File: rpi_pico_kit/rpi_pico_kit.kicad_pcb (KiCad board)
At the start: 2 copper layers, 244 parts, among them J1 DC Jack 5.5x2.1mm, J10 OLED Display SSD1306, J11 Conn_01x04_Male, J12 Conn_01x04_Male, J13 AudioJack-CUI-SJ-3523-SMT, J14 AudioJack-CUI-SJ-3523-SMT, J2 USB_B, J3 Conn_01x03_Male, J4 DB15_Female_HighDensity_Mount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, J5 HDMI_A, J6 Conn_01x08_Male, J7 Conn_01x08_Male, J8 Conn_01x08_Male, J9 Micro_SD_Card_Det, Q1 DMN63D8L-7, Q2 DMN63D8L-7, Q3 DMN63D8L-7, Q4 DMN63D8L-7, Q5 DMN63D8L-7, Q6 DMN63D8L-7, Q7 DMN63D8L-7, SW1 SW_Push, SW10 SW_Push, SW2 RotaryEncoder_Switch, SW3 SW_Push, SW4 SW_Push, SW5 SW_Push, SW6 SW_Push, SW7 SW_Push, SW8 SW_Push, SW9 SW_Push, U1 RPi Pico, U10 74LVC2G34GV, U11 PCM5101A, U2 NCP1117-3.3_SOT223, U3 RP2040, U4 W25Q16JVSSIQ, U5 74HC14, U6 74HC14, U7 MCP23S08-xSO, U8 AT24CS32, U9 NCP115-3.3_SOT23-5, Y1 12MHz

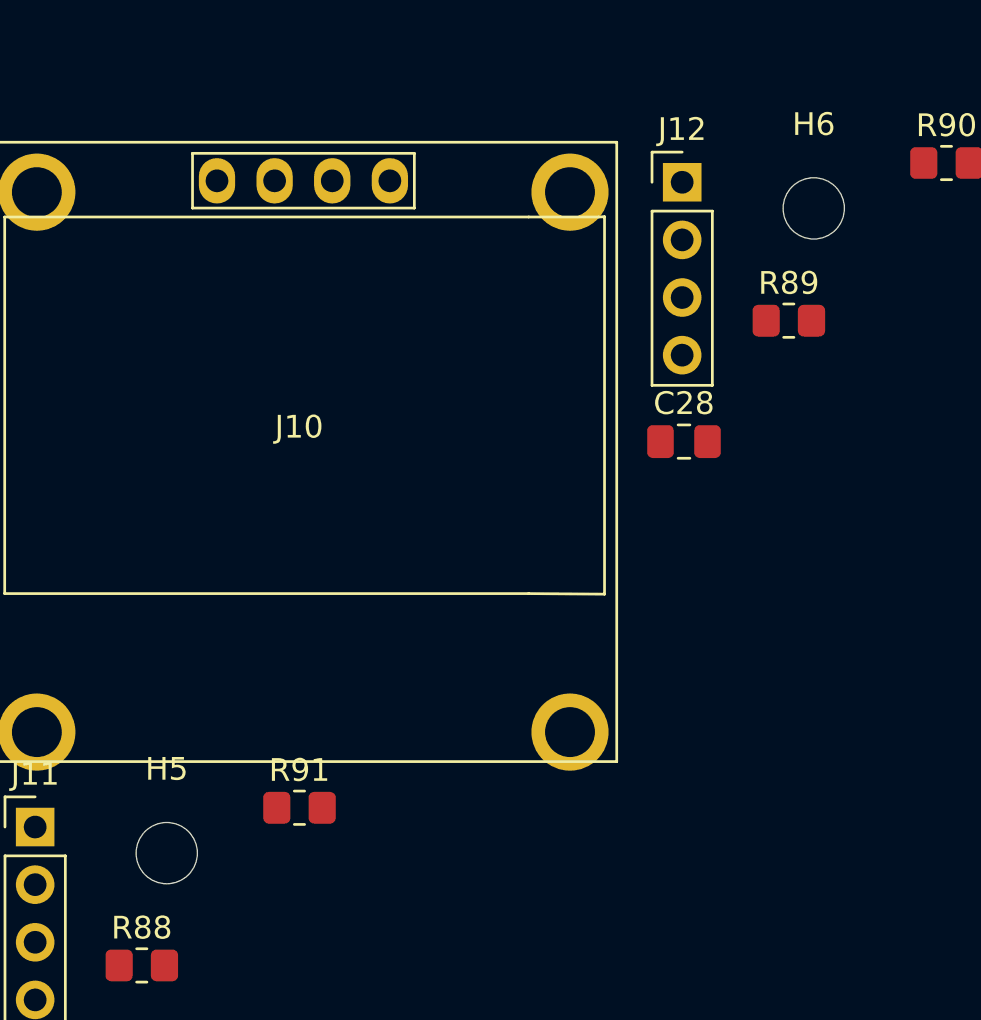
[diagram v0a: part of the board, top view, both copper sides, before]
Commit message: removed additional holes for oled
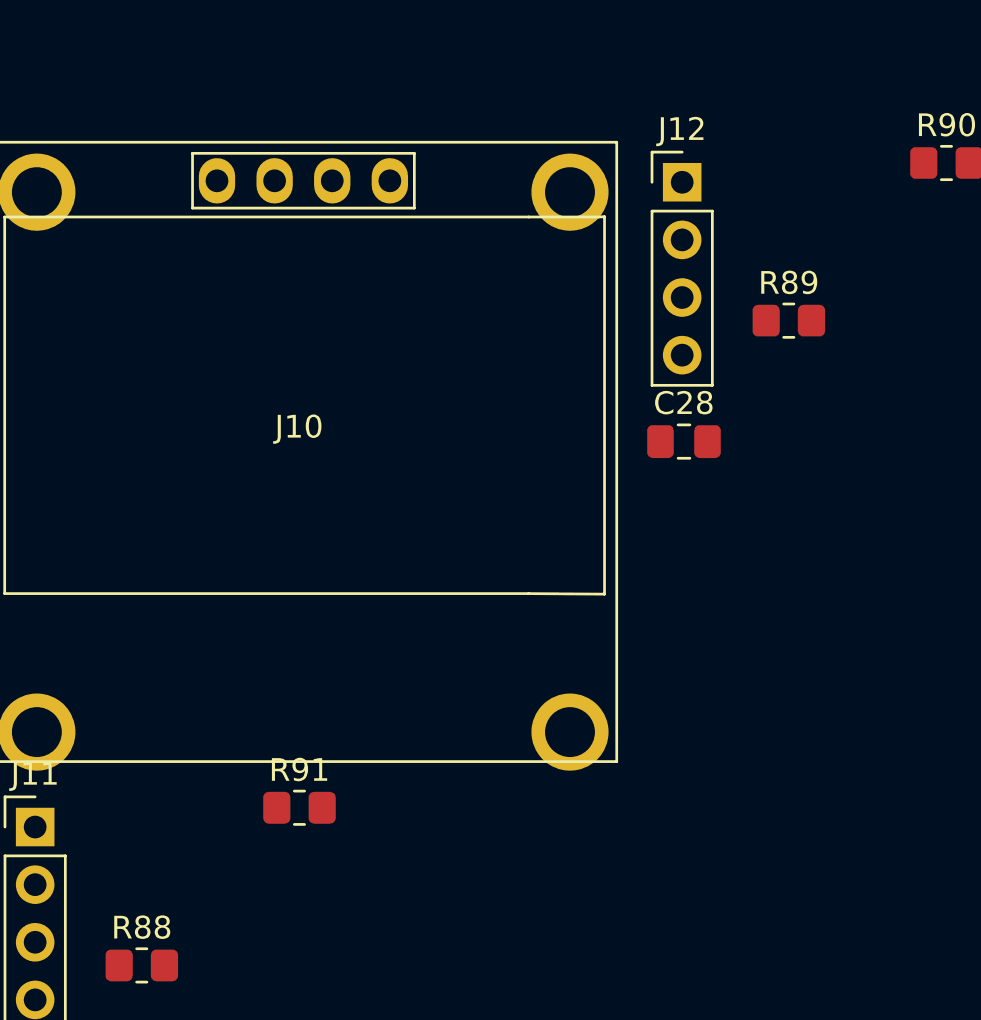
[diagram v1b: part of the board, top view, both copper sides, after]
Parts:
- removed H5, H6: MountingHole, MountingHole:MountingHole_2.7mm_M2.5
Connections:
- J10 pad 1: GND -> unconnected-(J10-GND)
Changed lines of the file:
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@@
   (net 210 "unconnected-(U7-INT)")
   (net 211 "unconnected-(U9-NC)")
+  (net 212 "unconnected-(J10-GND)")
   (footprint "Resistor_SMD:R_0805_2012Metric_Pad1.20x1.40mm_HandSolder" (layer "F.Cu")
     (at 158.5692 106.0422)
@@
     )
   )
-  (footprint "MountingHole:MountingHole_2.7mm_M2.5" (layer "F.Cu")
-    (at 177.1692 51.5222)
-    (descr "Mounting Hole 2.7mm, no annular, M2.5")
-    (tags "mounting hole 2.7mm no annular m2.5")
-    (property "Manufacturer Part Number" "~")
-    (property "Sheetfile" "i2c_devices.kicad_sch")
-    (property "Sheetname" "I2C Devices")
-    (property "Supplier" "~")
-    (property "Supplier Part URL" "~")
-    (attr exclude_from_pos_files)
-    (fp_text reference "H5" (at 0 -3.7) (layer "F.SilkS")
-        (effects (font (size 1 1) (thickness 0.15)))
-    )
-    (fp_text value "MountingHole" (at 0 3.7) (layer "F.Fab")
-        (effects (font (size 1 1) (thickness 0.15)))
-    )
-    (fp_text user "${REFERENCE}" (at 0 0) (layer "F.Fab")
-        (effects (font (size 1 1) (thickness 0.15)))
-    )
-    (fp_circle (center 0 0) (end 2.7 0)
-      (stroke (width 0.15) (type solid)) (fill none) (layer "Cmts.User"))
-    (fp_circle (center 0 0) (end 2.95 0)
-      (stroke (width 0.05) (type solid)) (fill none) (layer "F.CrtYd"))
-    (pad "" np_thru_hole circle (at 0 0) (size 2.7 2.7) (drill 2.7) (layers *.Cu *.Mask))
-  )
   (footprint "Custom:SW_SPST_Omron_B3FS-100xP_12" (layer "F.Cu")
     (at 34.6092 74.8622)
@@
     )
   )
-  (footprint "MountingHole:MountingHole_2.7mm_M2.5" (layer "F.Cu")
-    (at 205.6892 23.1022)
-    (descr "Mounting Hole 2.7mm, no annular, M2.5")
-    (tags "mounting hole 2.7mm no annular m2.5")
-    (property "Manufacturer Part Number" "~")
-    (property "Sheetfile" "i2c_devices.kicad_sch")
-    (property "Sheetname" "I2C Devices")
-    (property "Supplier" "~")
-    (property "Supplier Part URL" "~")
-    (attr exclude_from_pos_files)
-    (fp_text reference "H6" (at 0 -3.7) (layer "F.SilkS")
-        (effects (font (size 1 1) (thickness 0.15)))
-    )
-    (fp_text value "MountingHole" (at 0 3.7) (layer "F.Fab")
-        (effects (font (size 1 1) (thickness 0.15)))
-    )
-    (fp_text user "${REFERENCE}" (at 0 0) (layer "F.Fab")
-        (effects (font (size 1 1) (thickness 0.15)))
-    )
-    (fp_circle (center 0 0) (end 2.7 0)
-      (stroke (width 0.15) (type solid)) (fill none) (layer "Cmts.User"))
-    (fp_circle (center 0 0) (end 2.95 0)
-      (stroke (width 0.05) (type solid)) (fill none) (layer "F.CrtYd"))
-    (pad "" np_thru_hole circle (at 0 0) (size 2.7 2.7) (drill 2.7) (layers *.Cu *.Mask))
-  )
   (footprint "Connector_BarrelJack:BarrelJack_GCT_DCJ200-10-A_Horizontal" (layer "F.Cu")
     (at 62.5892 21.6522)
@@
       (stroke (width 0.05) (type default)) (fill none) (layer "F.CrtYd"))
     (pad "1" thru_hole oval (at -3.62 -10.6 90) (size 2 1.6) (drill 1) (layers *.Cu *.Mask)
-      (net 3 "GND") (pinfunction "GND") (pintype "input"))
+      (net 212 "unconnected-(J10-GND)") (pinfunction "GND") (pintype "input"))
     (pad "2" thru_hole oval (at -1.08 -10.6 90) (size 2 1.6) (drill 1) (layers *.Cu *.Mask)
       (net 1 "+3V3") (pinfunction "VCC") (pintype "input"))

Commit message: initial changes in pcb, drawn pcb outline
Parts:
- moved C1 390.2 mm to (-142.3, -0.30)
- moved C10 390.2 mm to (-150.6, 8.23)
- moved C11 390.2 mm to (-137.5, -0.30)
- moved C12 390.2 mm to (-142.3, 2.71)
- moved C13 390.2 mm to (-160.1, 16.0)
- moved C14 390.2 mm to (-140.8, -3.31)
- moved C15 390.2 mm to (-132.4, -8.86)
- moved C16 390.2 mm to (-160.1, 19.1)
- moved C17 390.2 mm to (-160.1, 22.1)
- moved C18 390.2 mm to (-155.3, 16.0)
- moved C2 390.2 mm to (-127.6, -8.86)
- moved C3 390.2 mm to (-157.3, 11.1)
- moved C4 390.2 mm to (-145.8, 8.23)
- moved C5 390.2 mm to (-169.4, 33.5)
- moved C6 390.2 mm to (-136.0, -3.31)
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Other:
- board outline added: 149.9 x 99.1 mm

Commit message: filtered controls and indicators
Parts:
- moved J14 294.0 mm to (129.5, 74.2)
- moved SW9 287.7 mm to (102.2, 130.2)
- moved J10 279.7 mm to (167.0, 68.6)
- moved J13 278.3 mm to (115.2, 74.8)
- moved SW10 269.8 mm to (116.2, 130.2)
- moved LED5 262.5 mm to (161.9, 113.0)
- moved J11 259.5 mm to (144.8, 114.9)
- moved SW5 257.7 mm to (156.8, 131.4)
- moved SW6 253.4 mm to (168.9, 131.4)
- moved J9 253.1 mm to (84.5, 105.1)
- moved SW4 246.0 mm to (144.8, 131.4)
- moved SW7 245.5 mm to (75.6, 130.2)
- moved BZ1 244.2 mm to (90.2, 76.2)
- moved LED7 242.5 mm to (161.9, 120.7)
- moved J2 241.0 mm to (66.1, 49.7), turned to 90 degrees
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
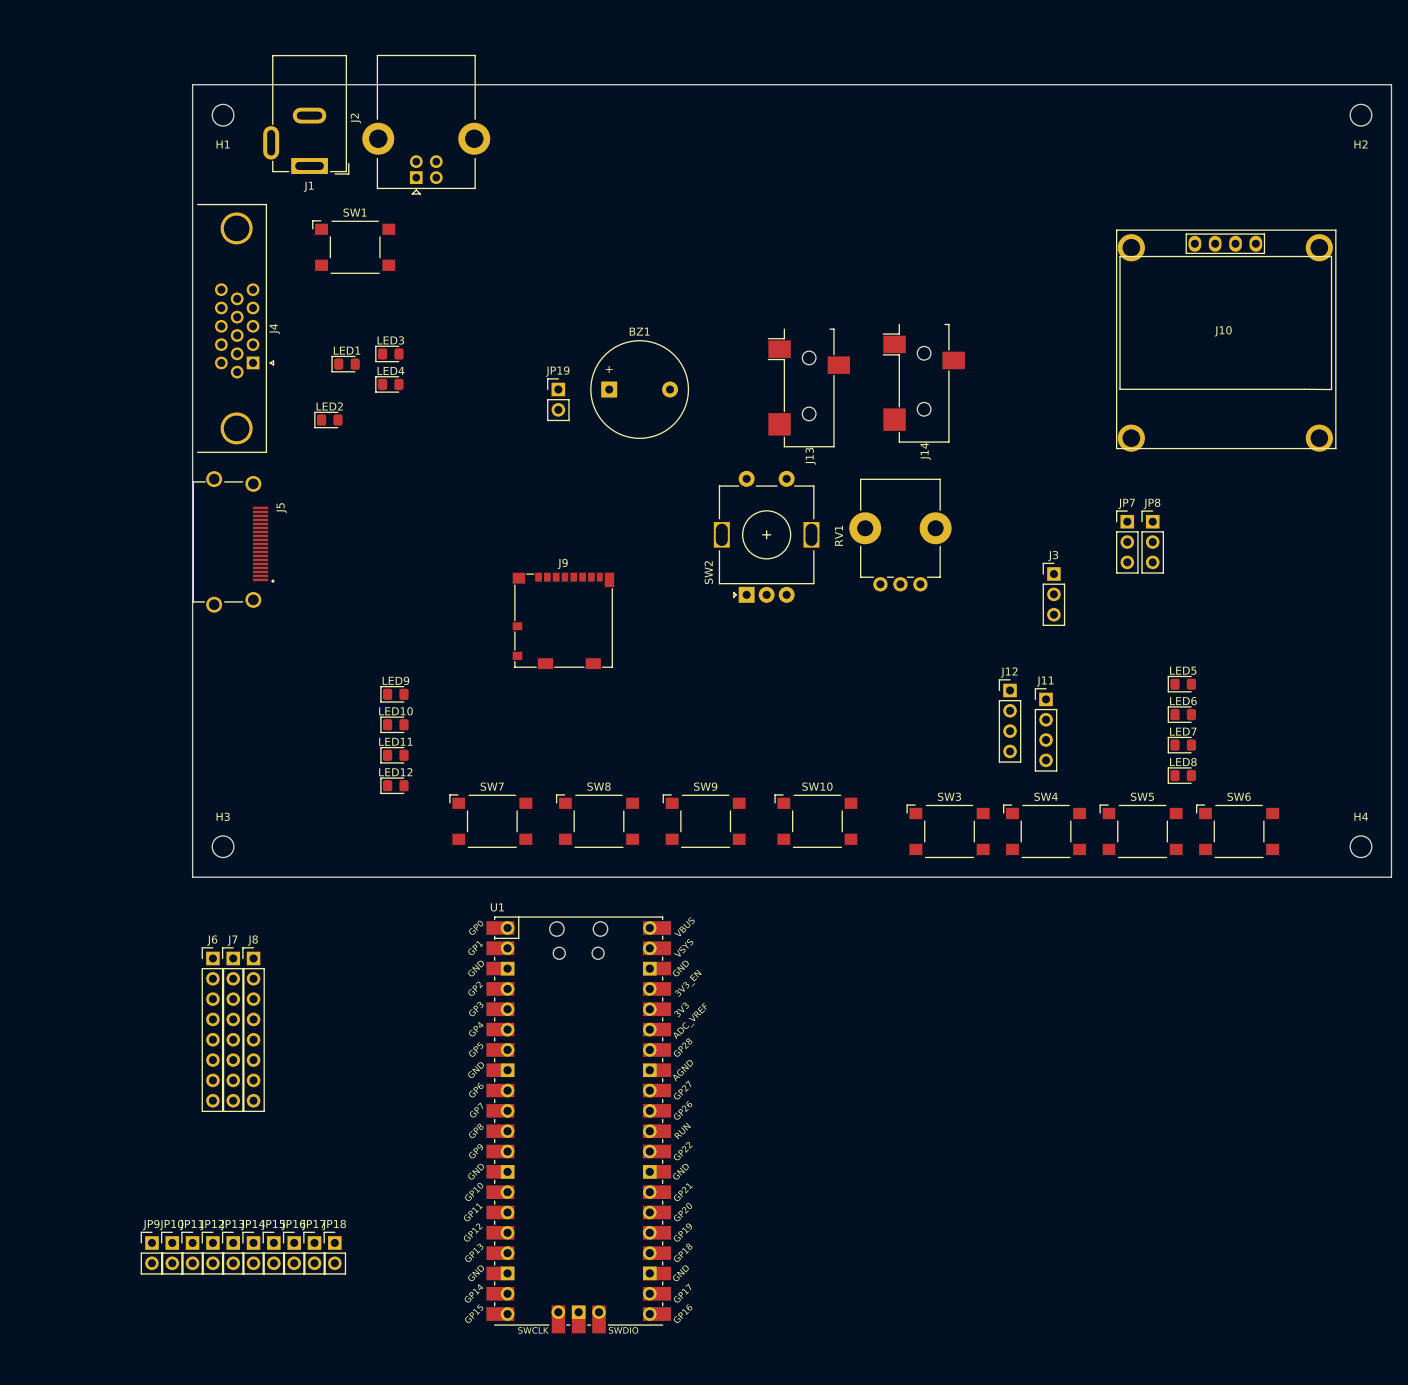
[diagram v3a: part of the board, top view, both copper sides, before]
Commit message: changed position of controls and indicators
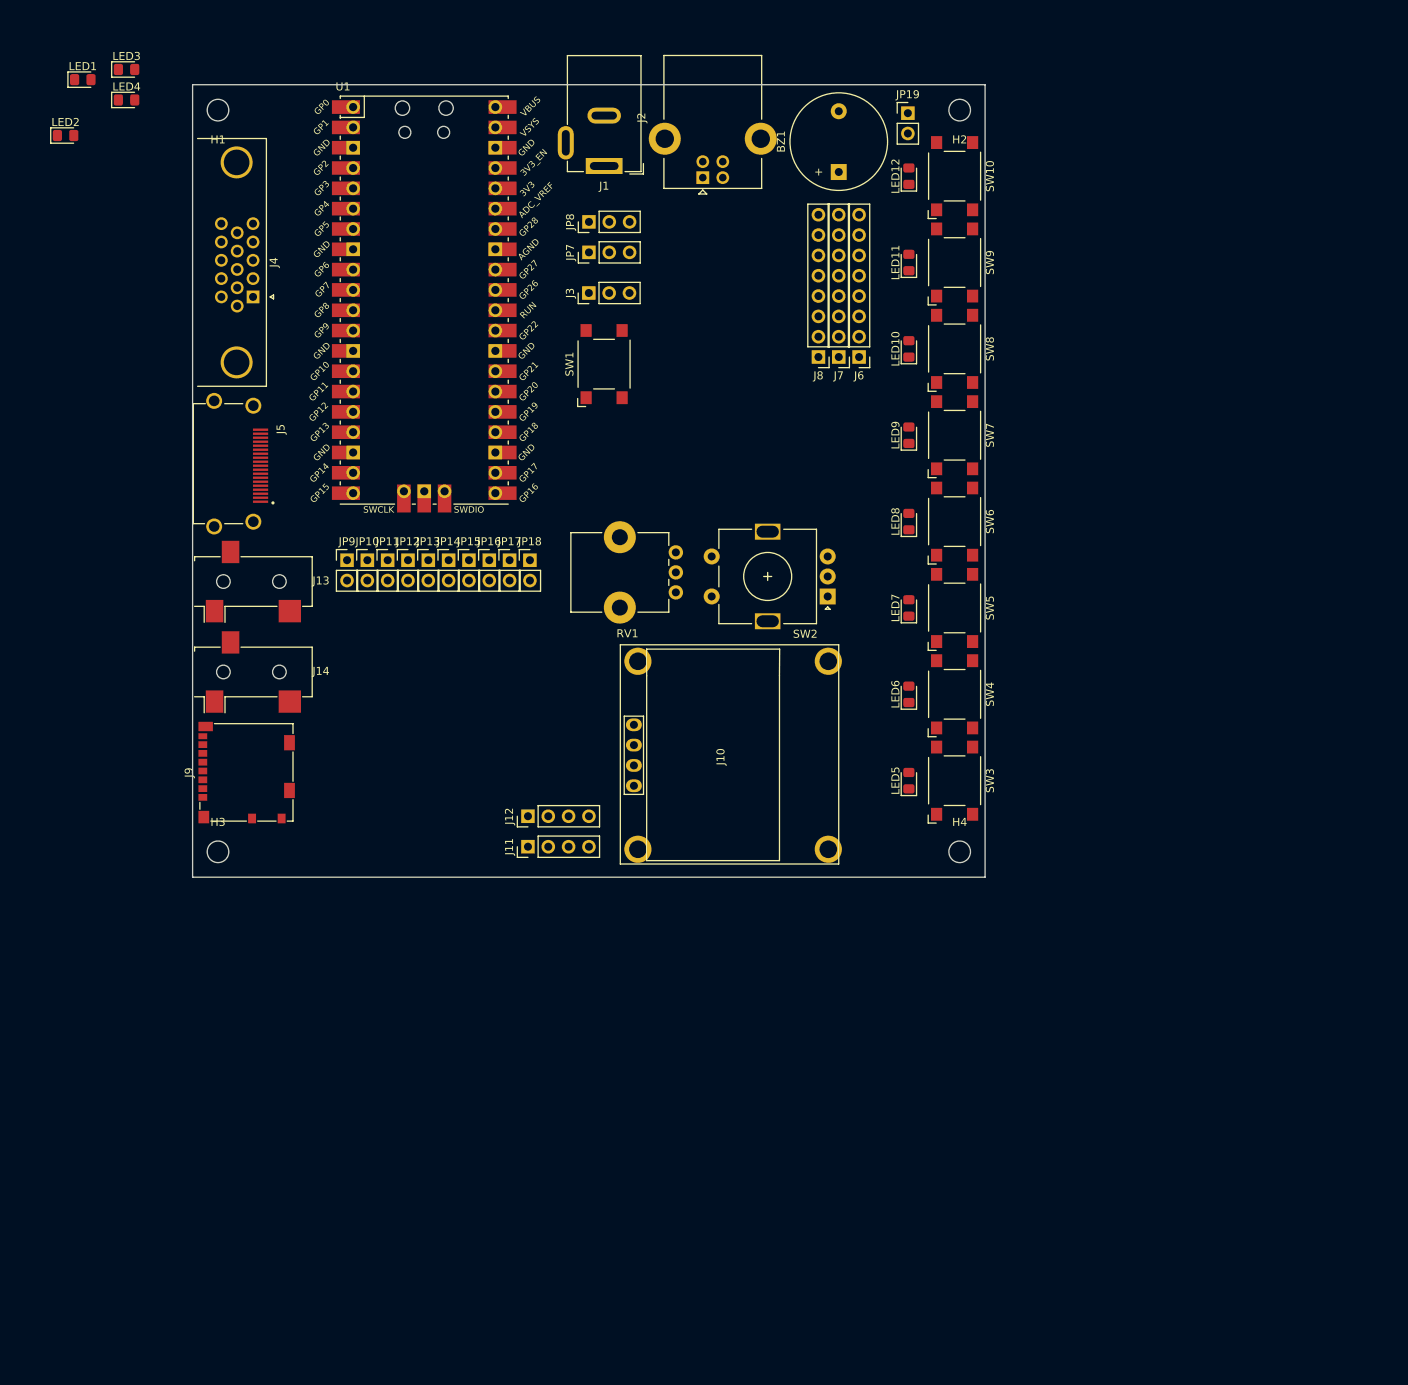
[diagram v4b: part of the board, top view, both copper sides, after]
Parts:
- moved J6 110.3 mm to (121.4, 72.1), turned to 180 degrees
- moved J7 106.7 mm to (118.9, 72.1), turned to 180 degrees
- moved U1 104.4 mm to (67.1, 65.0)
- moved J8 103.1 mm to (116.3, 72.1), turned to 180 degrees
- moved LED12 99.6 mm to (127.6, 49.5), turned to 90 degrees
- moved J14 92.9 mm to (44.5, 111.5), turned to 90 degrees
- moved LED11 88.9 mm to (127.6, 60.3), turned to 90 degrees
- moved JP10 88.8 mm to (59.9, 97.5)
- moved JP11 88.8 mm to (62.5, 97.5)
- moved JP12 88.8 mm to (65.0, 97.5)
- moved JP13 88.8 mm to (67.6, 97.5)
- moved JP14 88.8 mm to (70.1, 97.5)
- moved JP15 88.8 mm to (72.6, 97.5)
- moved JP16 88.8 mm to (75.2, 97.5)
- moved JP17 88.8 mm to (77.7, 97.5)
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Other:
- board size 149.9 x 99.1 mm -> 99.1 x 99.1 mm

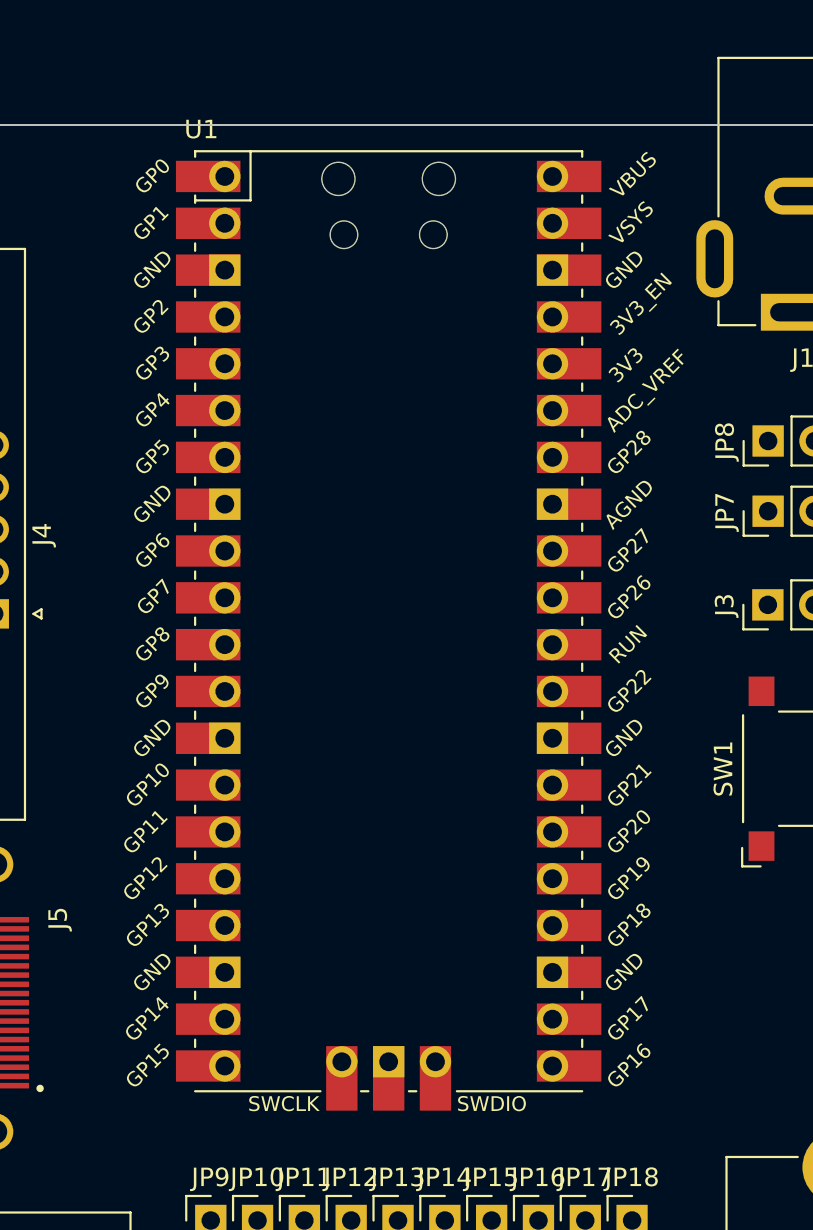
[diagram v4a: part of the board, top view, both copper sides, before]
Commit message: changed rpi pico footprint in project
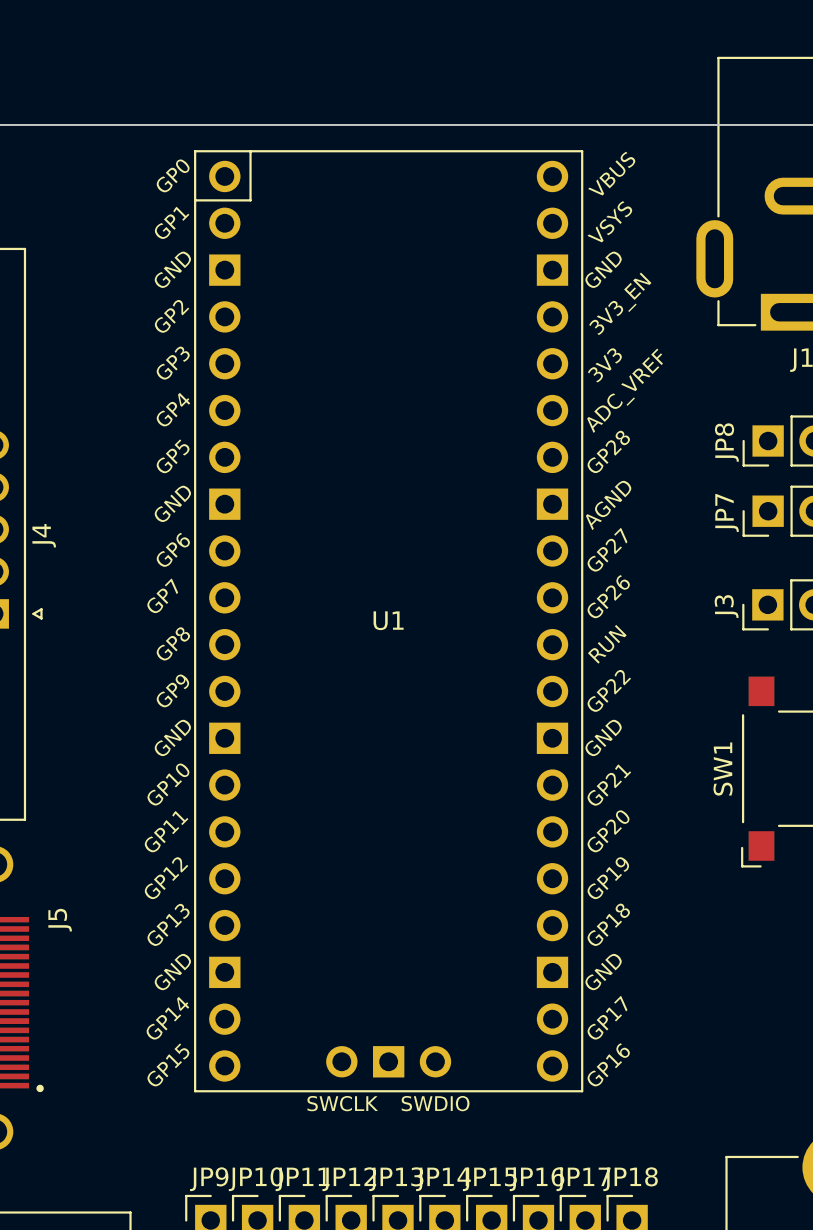
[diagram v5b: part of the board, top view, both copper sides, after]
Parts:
- U1: footprint RPi_Pico:RPi_Pico_SMD_TH -> RPi_Pico:RPi_Pico_THT
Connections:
- J10 pad 1: unconnected-(J10-GND) -> GND
